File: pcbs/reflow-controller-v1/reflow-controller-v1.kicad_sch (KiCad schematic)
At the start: 9 parts, among them J101 EB163A-03-C-180, J102 EB163A-02-C-180, J103 EB163A-02-C-180, J104 EB163A-02-C-180, J105 EB163A-02-C-180, J106 PinHeader 1x03 P2.54mm, M101 47053-1000

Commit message: added temp sensor
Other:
- added sheet Temperature onboard 1 (temp_sensor_onboard.kicad_sch)
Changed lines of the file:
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@@
+    )
+  )
+  (sheet (at 98.425 179.705) (size 24.765 12.065) (fields_autoplaced)
+    (stroke (width 0.1524) (type solid))
+    (fill (color 0 0 0 0.0000))
+    (property "Sheetname" "Temperature onboard 1" (at 98.425 178.9934 0)
+      (effects (font (size 1.27 1.27)) (justify left bottom))
+    )
+    (property "Sheetfile" "temp_sensor_onboard.kicad_sch" (at 98.425 192.3546 0)
+      (effects (font (size 1.27 1.27)) (justify left top))
+    )
+    (pin "SCL" input (at 123.19 182.88 0)
+      (effects (font (size 1.27 1.27)) (justify right))
+    )
+    (pin "SDA" bidirectional (at 123.19 185.42 0)
+      (effects (font (size 1.27 1.27)) (justify right))
+    )
+    (instances
+      (project "reflow-controller-v1"
+        (path "/843848ae-bf49-42cb-8f8b-76790d2e568d" (page "14"))
+      )
     )
   )

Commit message: kicad version bump
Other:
- added sheet microcontroller (microcontroller.kicad_sch)

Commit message: footprint assignement fixed; buzzer added
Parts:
- added J1: PinHeader 1x03 P2.54mm, Connector_PinHeader_2.54mm:PinHeader_1x03_P2.54mm_Vertical, symbol Connector_Generic:Conn_01x03
- F101, F102: value Fuse -> Schurter 0031.8221; footprint (none) -> Fuse:Fuseholder_Cylinder-5x20mm_Schurter_OGN-SMD_Horizontal_Open
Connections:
- net +5V: now also J1.2 (Pin_2)
- net GND: now also J1.1 (Pin_1)
- net Servo renamed Servo1
- new net Servo2: J1.3 (Pin_3)
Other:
- moved on the sheet: M101

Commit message: add debug power input
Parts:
- added J3: PinHeader 1x02 P2.54mm, Connector_PinHeader_2.54mm:PinHeader_1x02_P2.54mm_Vertical, symbol Connector_Generic:Conn_01x02
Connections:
- net +5V: now also J3.1 (Pin_1)
- net GND: now also J3.2 (Pin_2)
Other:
- note added: "Debug Power In"

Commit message: WIP pcb design & routing
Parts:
- removed J3: PinHeader 1x02 P2.54mm, Connector_PinHeader_2.54mm:PinHeader_1x02_P2.54mm_Vertical, symbol Connector_Generic:Conn_01x02
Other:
- sheet Buttons ports: added Buzzer; removed none
- sheet Display LCD ports: added SD_MISO, SD_MOSI, SD_SCK, Touch; removed none
- sheet microcontroller ports: added BTN_1, BTN_2, Buzzer, DISP_LED, Display_SPI_DC/RS, Display_SPI_MISO, Display_SPI_MOSI, Display_SPI_SCK, Encoder_A, Encoder_B, LED_green, LED_red, OLED1_I2C_SCL, OLED1_I2C_SDA, OLED2_I2C_SCL, OLED2_I2C_SDA, PWM_1, PWM_2, PWM_3, SD_MISO, SD_MOSI, SD_SCK, SSR1, SSR2, SSR3, SSR4, SW_Encoder, Temp_I2C_SCL, Temp_I2C_SDA, Temp_SPI_MISO, Temp_SPI_MOSI, Temp_SPI_SCK, Touch, Touch_SPI_CS, Touch_SPI_IRQ, Touch_SPI_MISO, Touch_SPI_MOSI, Touch_SPI_SCK, ~{Display_CS}, ~{Display_RESET}, ~{Temp_CS1}, ~{Temp_CS2}, ~{Temp_CS3}, ~{Temp_DRDY1}, ~{Temp_DRDY2}, ~{Temp_DRDY3}; removed none
- note removed: "Debug Power In"

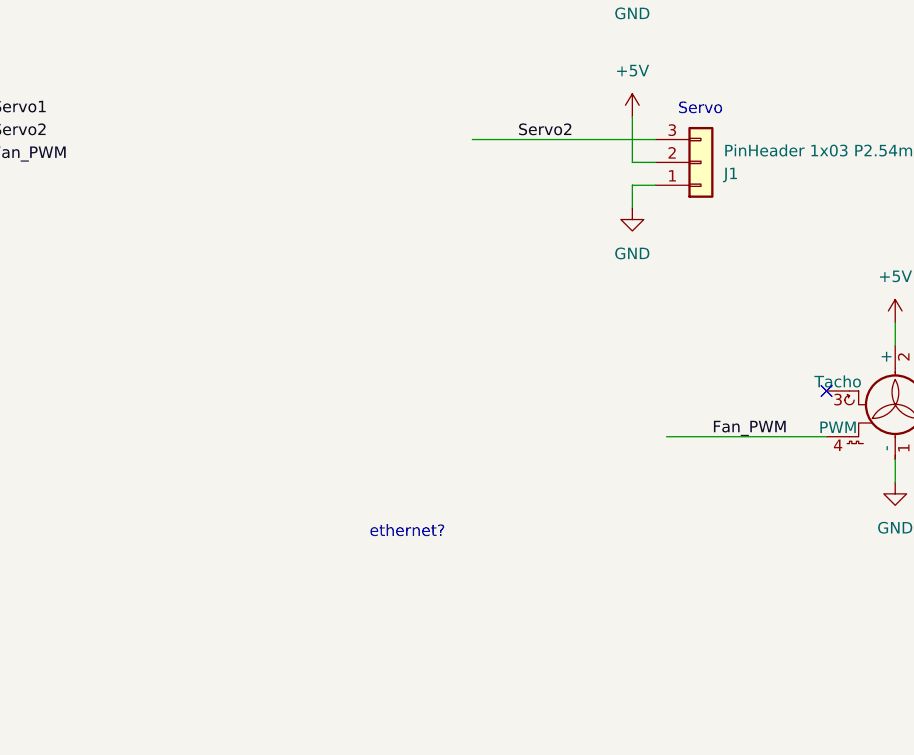
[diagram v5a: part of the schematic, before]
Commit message: update routing with new mechanical positioning
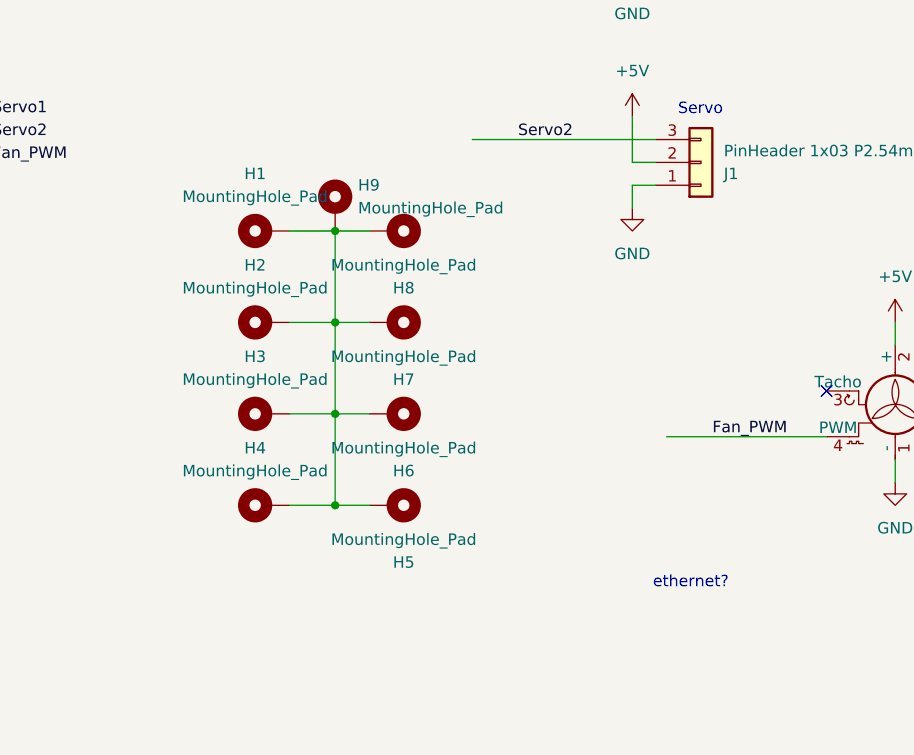
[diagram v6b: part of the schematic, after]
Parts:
- added H1, H2, H3, H4, H5, H6, H7, H8, H9: MountingHole_Pad, Mounting_Wuerth:Mounting_Wuerth_WA-SMSI-M3_H15mm_9774150360, symbol Mechanical:MountingHole_Pad
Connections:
- new net: H1.1, H2.1, H3.1, H4.1, H5.1, H6.1, H7.1, H8.1, H9.1
